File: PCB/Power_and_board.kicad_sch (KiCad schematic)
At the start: 20 parts, among them J7 PWR_HEADER, U1 AMS1117-3.3

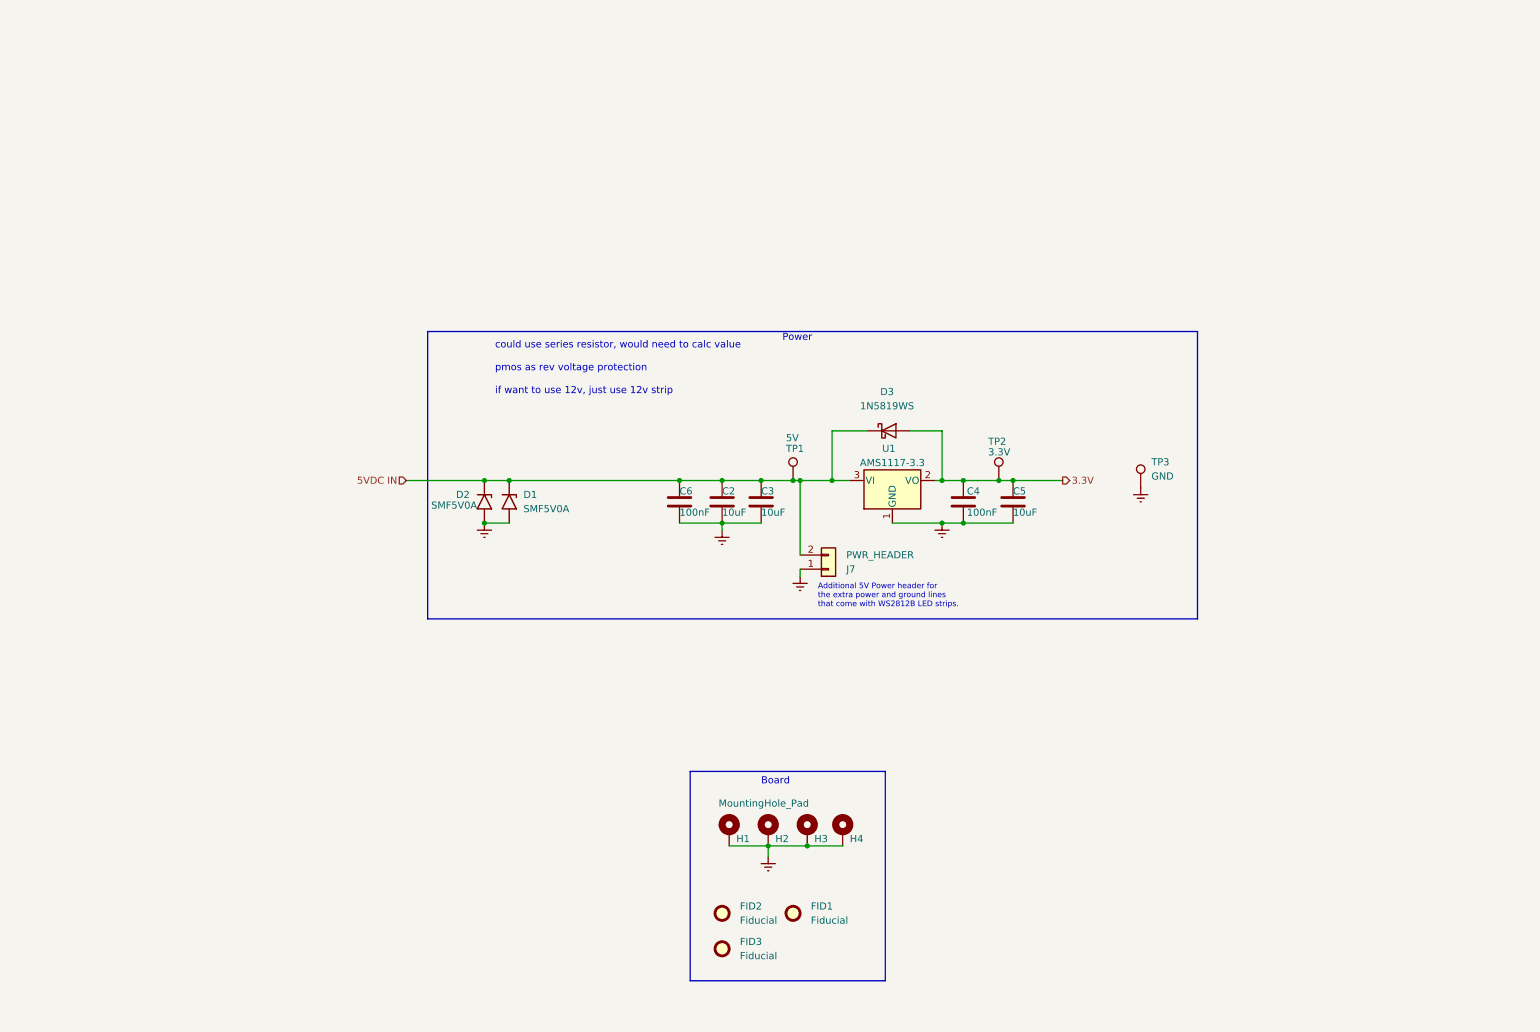
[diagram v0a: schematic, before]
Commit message: Major schematic update for v2.3
This was my first real PCB project, and looking back with a couple
months of hindsight I made some mistakes. Some best practices for
driving WS2812B strips weren't followed in my original version, and
I've updated the schematic to reflect what I've learned and what
improvements needed to be made.

* Warning added to README about current version
* Schematic reorganized into tiles
* RTC clock removed
* OLED and I2C headers removed
* JTAG footprint updated
* Pin header output replaced with screw terminal
* Hole size for power injection header increased
* Added whole system fuse and PTC fuse to protect ESP32
* Added reverse polarity protection and re-added ability to disconnect
  USB Vbus from Vdd, so it's possible to program when the strip is
  connected to 12V without frying your computer

There are a couple other improvements that could still be made to the
schematic (removing the solderwire connector for example) but it remains to
be seen if I'm going to go back and re-design the PCB to incorporate
these changes or move onto newer projects.
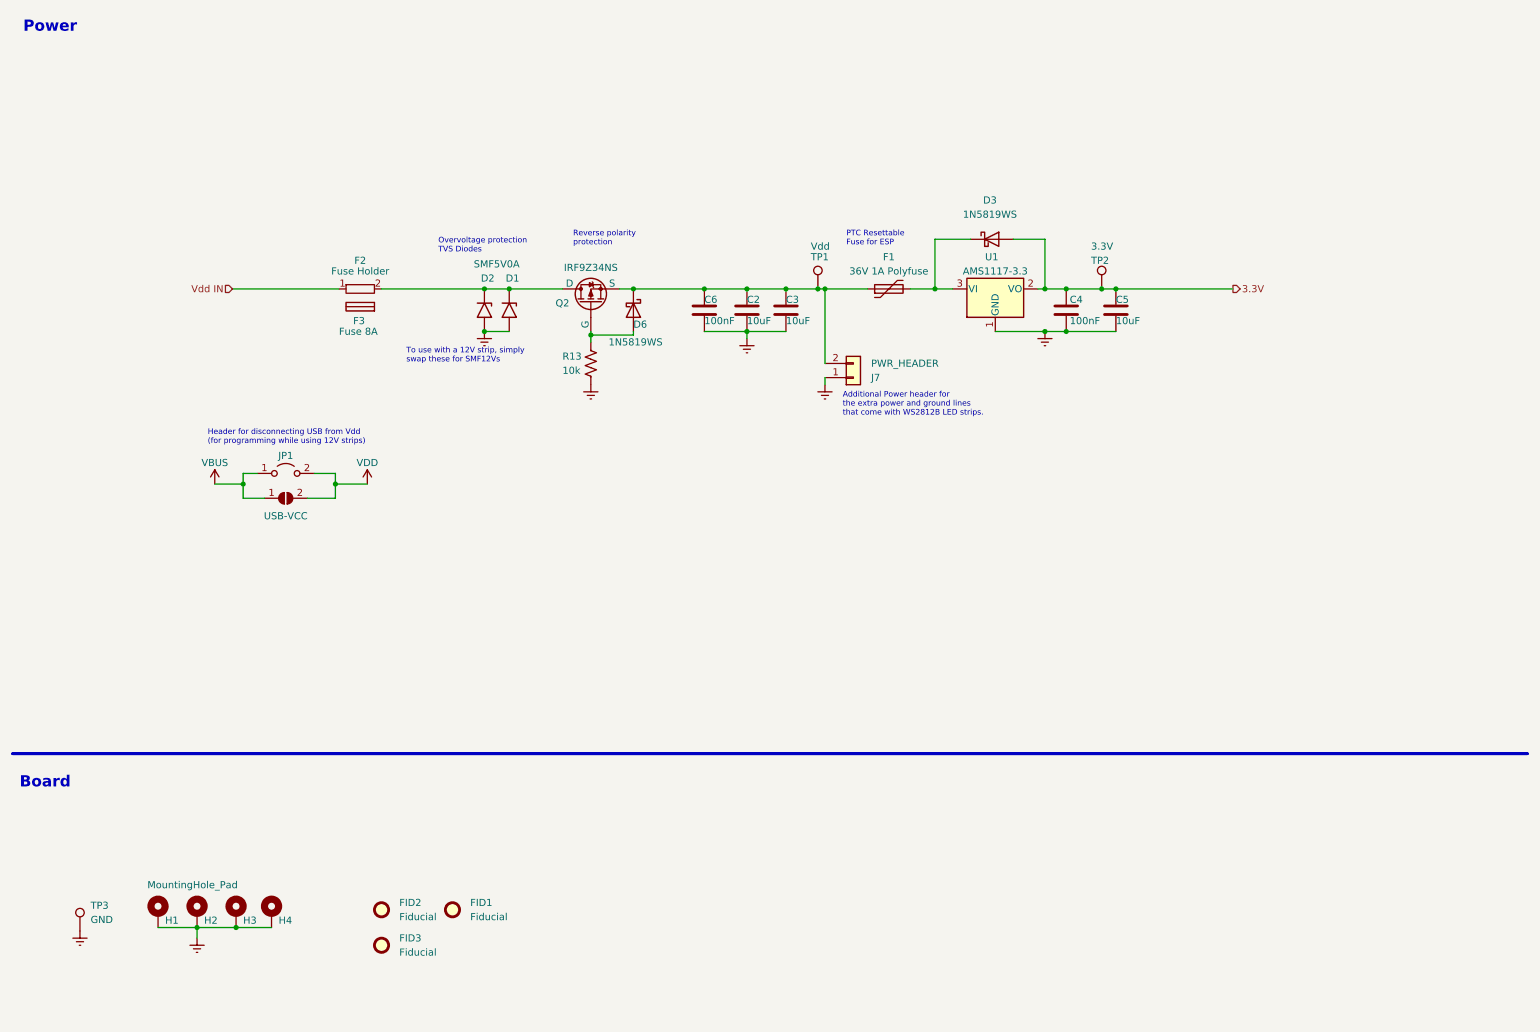
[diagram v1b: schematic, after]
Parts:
- added D6: 1N5819WS, Diode_SMD:D_SOD-323_HandSoldering, symbol Device:D_Schottky
- added F1: 36V 1A Polyfuse, Fuse:Fuse_1206_3216Metric_Pad1.42x1.75mm_HandSolder, symbol Device:Polyfuse
- added F2: Fuse Holder, jmux-footprints:FUSE-TH_XF-505P, symbol projectlib:FuseHolder
- added F3: Fuse 8A, symbol projectlib:Fuse-noLegs
- added JP1: Jumper_2_Open, TestPoint:TestPoint_2Pads_Pitch2.54mm_Drill0.8mm, symbol Jumper:Jumper_2_Open
- added JP3: USB-VCC, Jumper:SolderJumper-2_P1.3mm_Open_RoundedPad1.0x1.5mm, symbol Jumper:SolderJumper_2_Open
- added Q2: IRF9Z34NS, Package_TO_SOT_SMD:TO-263-2, symbol Simulation_SPICE:PMOS
- added R13: 10k, Resistor_SMD:R_0805_2012Metric_Pad1.20x1.40mm_HandSolder, symbol Device:R_US
- J7: footprint Connector_Wire:SolderWire-0.1sqmm_1x02_P3.6mm_D0.4mm_OD1mm -> Connector_Wire:SolderWire-0.5sqmm_1x02_P4.6mm_D0.9mm_OD2.1mm
- TP1: value 5V -> Vdd
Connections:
- net Earth: now also R13.2
- net 5VDC IN: no longer names the net of C2.1, C3.1, C6.1, J7.2 (Pin_2), TP1.1
- net 5VDC IN: now also D6.1 (K), F1.1, Q2.3 (S); no longer D1.1 (A1), D2.1 (A1), D3.1 (K), U1.3 (VI)
- new net: D1.1 (A1), D2.1 (A1), F2.2, Q2.1 (D)
- new net: D3.1 (K), F1.2, U1.3 (VI)
- new net: D6.2 (A), Q2.2 (G), R13.1
- new net VBUS: JP1.1 (A), JP3.1 (A)
- new net VDD: JP1.2 (B), JP3.2 (B)
- new net Vdd IN: F2.1
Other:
- note added: "Additional Power header for the extra power and ground lines that come with WS2812B LED strips."
- note added: "Header for disconnecting USB from Vdd (for programming while using 12V strips)"
- note added: "Overvoltage protection TVS Diodes"
- note added: "PTC Resettable Fuse for ESP"
- note added: "Reverse polarity protection"
- note added: "To use with a 12V strip, simply swap these for SMF12Vs"
- note removed: "Additional 5V Power header for the extra power and ground lines that come with WS2812B LED strips."
- note removed: "could use series resistor, would need to calc value pmos as rev voltage protection if want to use 12v, just use 12v strip"
- company: (none) -> iotled.jacobbokor.com
- moved on the sheet: C2, C3, C4, C5, C6, D1, D2, D3, FID1, FID2, FID3, H1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

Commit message: Schematic and Board redesigned for new rev: v3.0
Schematic and board redone for next generation board - v3.0. Current rev is v3.0b.

* pin numbers added to PCB
* Silkscreen spot for writing board identifier in sharpie
* Silkscreen updated with more detailed information about board and pins to improve UX

* Logic level converters still present on data lines
* Selectable data line resistors added
* Moved to screw terminals instead of requiring soldered on connectors
* Logic level shifter IC - 74AHCT125 - Added. Two channels in use, one broken out to pads.

* System blade fuse added, along with PTC fuse for ESP itself.
* selectable board voltage - 5 or 12V
* Power inejction headers upgraded - board can be powered
    externally, or can be used as an (unfused) source of power for other LEDs!
* 5V LDO added to support logic level shifter IC

Kicad project library format changed based on since-gained kicad experience
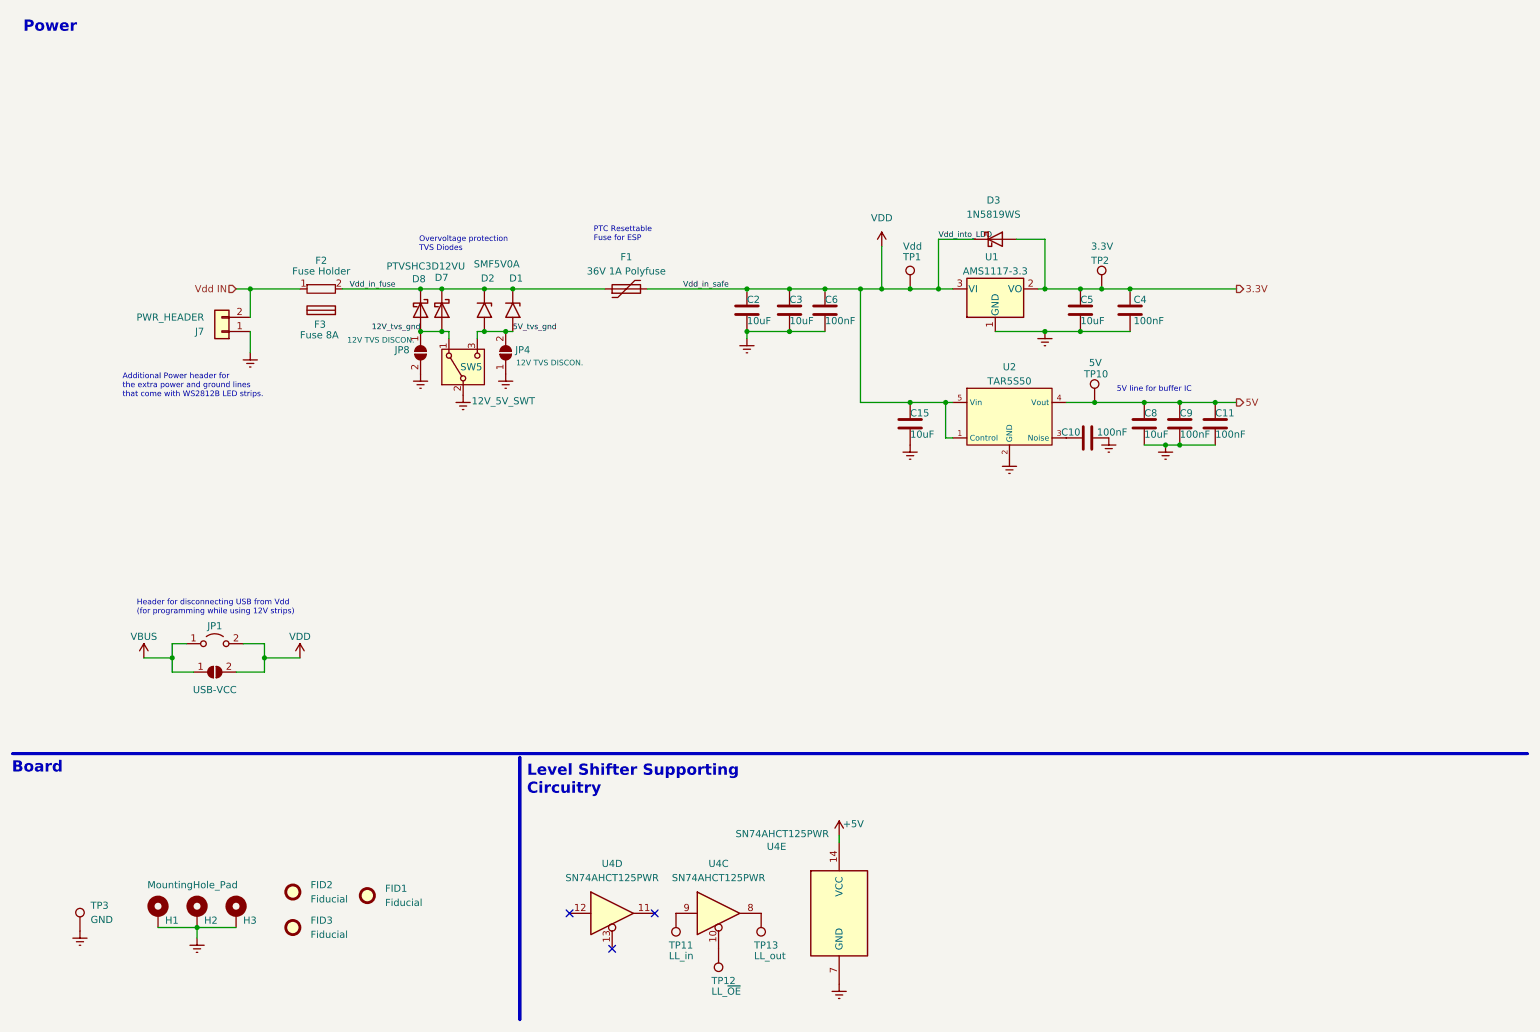
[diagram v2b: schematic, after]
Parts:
- removed D6: 1N5819WS, Diode_SMD:D_SOD-323_HandSoldering, symbol Device:D_Schottky
- removed H4: MountingHole_Pad, MountingHole:MountingHole_2.2mm_M2_Pad_Via, symbol Mechanical:MountingHole_Pad
- removed Q2: IRF9Z34NS, Package_TO_SOT_SMD:TO-263-2, symbol Simulation_SPICE:PMOS
- removed R13: 10k, Resistor_SMD:R_0805_2012Metric_Pad1.20x1.40mm_HandSolder, symbol Device:R_US
- added C10, C11, C9: 100nF, Capacitor_SMD:C_0805_2012Metric_Pad1.18x1.45mm_HandSolder, symbol Device:C
- added C15, C8: 10uF, Capacitor_SMD:C_0805_2012Metric_Pad1.18x1.45mm_HandSolder, symbol Device:C
- added D7, D8: PTVSHC3D12VU, Diode_SMD:D_SOD-323_HandSoldering, symbol Device:D_Schottky
- added JP4, JP8: 12V TVS DISCON., Jumper:SolderJumper-2_P1.3mm_Open_RoundedPad1.0x1.5mm, symbol Jumper:SolderJumper_2_Open
- added SW5: 12V_5V_SWT, Button_Switch_SMD:SW_SPDT_PCM12, symbol Switch:SW_SPDT
- added TP10: 5V, TestPoint:TestPoint_Pad_D1.5mm, symbol Connector:TestPoint
- added TP11: LL_in, TestPoint:TestPoint_Pad_D1.0mm, symbol Connector:TestPoint
- added TP12: LL_~{OE}, TestPoint:TestPoint_Pad_D1.0mm, symbol Connector:TestPoint
- added TP13: LL_out, TestPoint:TestPoint_Pad_D1.0mm, symbol Connector:TestPoint
- added U2: TAR5S50, projectlib:SSOP-5_L2.9-W1.6-P0.95-LS2.8-TL, symbol projectlib:TAR5S50
- added U4: SN74AHCT125PWR, Package_SO:TSSOP-14_4.4x5mm_P0.65mm, symbol 74xx:74AHCT125
- JP1: value Jumper_2_Open -> USB-VDD
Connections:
- net Earth: now also C10.2, C11.2, C15.2, C8.2, C9.2, JP4.1 (A), JP8.2 (B), SW5.2 (B), U2.2 (GND), U4.7 (GND); no longer D1.2 (A2), D2.2 (A2)
- net VDD: now also C2.1, C3.1, C6.1, D3.1 (K), F1.2, TP1.1, U1.3 (VI), C15.1, U2.1 (Control), U2.5 (Vin)
- net Vdd IN: now also J7.2 (Pin_2)
- net Vdd_in_fuse: now reaches D1.1 (A1), D2.1 (A1), F2.2
- net Vdd_in_fuse: now also F1.1, D7.1 (K), D8.1 (K)
- new net: TP11.1, U4.9
- new net: TP12.1, U4.10
- new net: C10.1, U2.3 (Noise)
- new net: TP13.1, U4.8
- new net +5V: U4.14 (VCC)
- new net 12V_tvs_gnd: D7.2 (A), D8.2 (A), JP8.1 (A), SW5.1 (A)
- new net 5V: C11.1, C8.1, C9.1, TP10.1, U2.4 (Vout)
- new net 5V_tvs_gnd: D1.2 (A2), D2.2 (A2), JP4.2 (B), SW5.3 (C)
- no-connect marks 0 -> 3
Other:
- note added: "5V line for buffer IC"
- note added: "Level Shifter Supporting Circuitry"
- note removed: "Reverse polarity protection"
- note removed: "To use with a 12V strip, simply swap these for SMF12Vs"
- title: Spotify Neopixel Visualizer -> IoT LEDDriver HW
- moved on the sheet: C3, C4, C5, C6, D1, D3, F1, F2, F3, FID2, FID3, J7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

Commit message: v3.2 changes
* Removed PTC fuse, since that caused issues on the last one
* Other minor changes (that i've forgotten)
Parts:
- added C16, C17: 10uF, Capacitor_SMD:C_0805_2012Metric_Pad1.18x1.45mm_HandSolder, symbol Device:C
- added C18: 100nF, Capacitor_SMD:C_0805_2012Metric_Pad1.18x1.45mm_HandSolder, symbol Device:C
- added D6: 1N4148W, Diode_SMD:D_SOD-123, symbol Diode:1N4148W
- added K2: SANYOU_SRD_Form_C, Relay_THT:Relay_SPDT_SANYOU_SRD_Series_Form_C, symbol Relay:SANYOU_SRD_Form_C
- added Q1: AO3400A, Package_TO_SOT_SMD:SOT-23_Handsoldering, symbol Transistor_FET:AO3400A
- added R1: 10k, Resistor_SMD:R_0805_2012Metric_Pad1.20x1.40mm_HandSolder, symbol Device:R_US
- F1: Vendor (none) -> https://www.lcsc.com/product-detail/Resettable-Fuses_LUTE-1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; now not fitted; now left out of the parts list
- F3: value Fuse 8A -> Fuse 10A
- JP4: value 12V TVS DISCON. -> 5V TVS DISCON.
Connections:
- net +5V is gone; now on net 5V: U4.14 (VCC)
- net 5V: now also D6.1 (K), K2.5
- net Earth: now also C16.2, C17.2, C18.2, Q1.2 (S), R1.1
- net VDD: now also C16.1, K2.3; no longer C15.1, C2.1, C3.1, C6.1, D3.1 (K), F1.2, JP1.2 (B), JP3.2 (B), TP1.1, U1.3 (VI), U2.1 (Control), U2.5 (Vin)
- net Vdd_in_fuse: now also C15.1, C2.1, C3.1, C6.1, D3.1 (K), JP1.2 (B), JP3.2 (B), TP1.1, U1.3 (VI), U2.1 (Control), U2.5 (Vin), C17.1, C18.1, K2.1; no longer F1.1
- new net: D6.2 (A), K2.2, Q1.3 (D)
- new net RELAY_PIN: Q1.1 (G), R1.2
- no-connect marks 3 -> 6
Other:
- note added: "MCU Power"
- note added: "Pre-Filtering and Overvoltage Protection"
- note added: "Relay Module"
- moved on the sheet: C10, C11, C15, C2, C3, C4, C5, C6, C8, C9, D1, D2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
